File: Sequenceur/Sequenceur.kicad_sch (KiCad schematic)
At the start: 50 parts, among them J1 AudioJack2, J2 Jack-DC, SW1 SW_Push, SW2 SW_Rotary12, U1 NE555P, U2 4017, U3 OP07

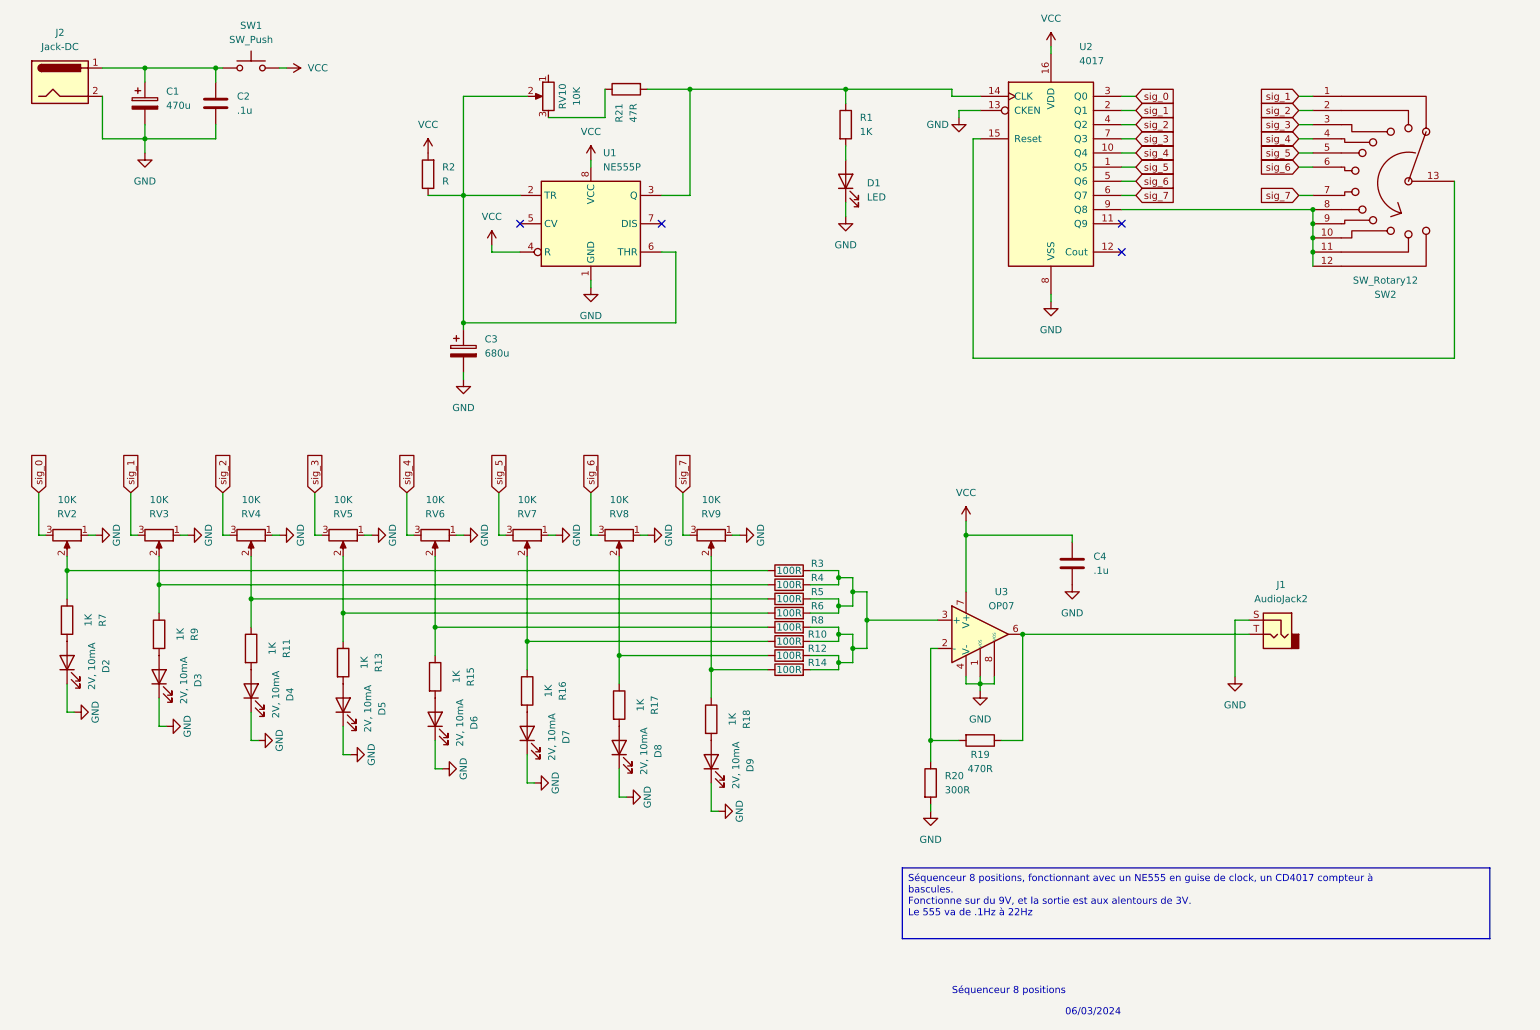
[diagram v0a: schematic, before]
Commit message: First real version of the PCB, as a 2 layer one, and with adapted footprints.
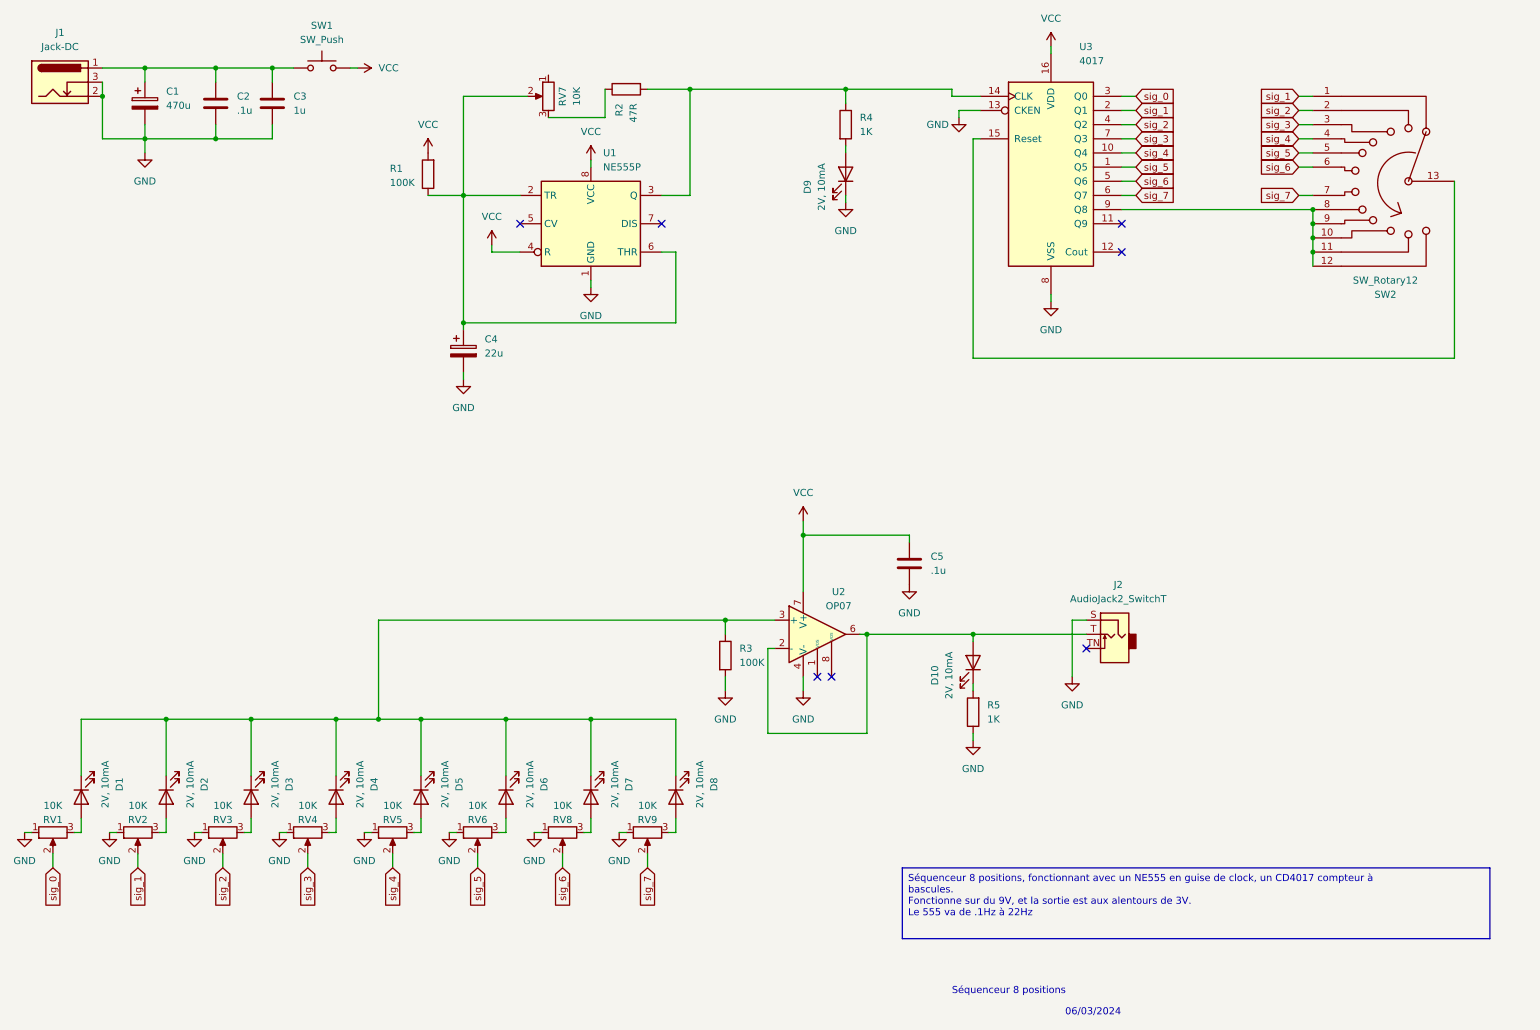
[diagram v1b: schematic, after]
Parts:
- removed D1: LED, LED_THT:LED_D3.0mm, symbol Device:LED
- removed J1: AudioJack2, Connector_Audio:Jack_6.35mm_Neutrik_NJ2FD-V_Vertical, symbol Connector_Audio:AudioJack2
- removed R10, R12, R14, R4, R6, R8: 100R, Resistor_SMD:R_0603_1608Metric, symbol Device:R
- removed R11, R13, R15, R16, R17, R18, R7, R9: 1K, Resistor_SMD:R_0603_1608Metric, symbol Device:R
- removed R19: 470R, Resistor_SMD:R_0805_2012Metric, symbol Device:R
- removed R20: 300R, Resistor_SMD:R_0805_2012Metric, symbol Device:R
- removed RV7: 10K, User_added:POTENTIOMETER_BOARDMNT_VERTICAL, symbol Device:R_Potentiometer
- added C3: 1u, Capacitor_SMD:C_0805_2012Metric, symbol Device:C
- added D10, D2: 2V, 10mA, LED_THT:LED_D5.0mm, symbol Device:LED
- added J2: AudioJack2_SwitchT, User_added:Jack_6.35_TTnS, symbol Connector_Audio:AudioJack2_SwitchT
- added RV2: 10K, User_added:POTENTIOMETER_BOARDMNT_VERTICAL, symbol Device:R_Potentiometer
- C4: renamed from C3; value 680u -> 22u; footprint Capacitor_THT:CP_Radial_D10.0mm_P5.00mm -> Capacitor_THT:CP_Radial_D5.0mm_P2.50mm
- D1: renamed from D2; footprint LED_THT:LED_D3.0mm -> LED_THT:LED_D5.0mm
- D3, D4, D5, D6, D7, D8, D9: footprint LED_THT:LED_D3.0mm -> LED_THT:LED_D5.0mm
- J1: renamed from J2; footprint Connector_BarrelJack:BarrelJack_SwitchcraftConxall_RAPC10U_Horizontal -> Connector_BarrelJack:BarrelJack_Horizontal; symbol Connector:Jack-DC -> Connector:Barrel_Jack_Switch
- R1: renamed from R2; value R -> 100K; footprint (none) -> Resistor_SMD:R_0603_1608Metric
- R3: value 100R -> 100K
- R5: value 100R -> 1K
- SW1: footprint User_added:PAD_2_std -> User_added:Switch_2pin
- renumbered C4 to C5, R21 to R2, R1 to R4, RV2 to RV1, RV10 to RV7, U3 to U2, U2 to U3
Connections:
- net GND: now also J1.3, R3.2, R5.1, C3.2, J2.S, RV2.1; no longer D1.1 (K), D3.1 (K), D4.1 (K), D5.1 (K), D6.1 (K), D7.1 (K), D8.1 (K), U2.1 (VOS), U2.8 (VOS)
- net sig_0: now also RV1.2; no longer RV1.3
- net sig_1: now also RV2.2; no longer RV3.3
- net sig_2: now also RV3.2; no longer RV4.3
- net sig_3: now also RV4.2; no longer RV5.3
- net sig_4: now also RV5.2; no longer RV6.3
- net sig_5: now also RV6.2
- net sig_6: now also RV8.2; no longer RV8.3
- net sig_7: now also RV9.2; no longer RV9.3
- net at R3.1: now also D1.1 (K), D3.1 (K), D4.1 (K), D5.1 (K), D6.1 (K), D7.1 (K), D8.1 (K), U2.3 (+), D2.1 (K); no longer RV1.2
- net at D4.2 (A): now also RV4.3
- net at D5.2 (A): now also RV5.3
- net at D7.2 (A): now also RV8.3
- net at D6.2 (A): now also RV6.3
- net at C1.1, C2.1, J1.1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: now also C3.1
- net at R4.2: now also D9.2 (A)
- net at U2.6: now also U2.2 (-), D10.2 (A), J2.T
- net at D8.2 (A): now also RV9.3
- net at D3.2 (A): now also RV3.3
- net at D1.2 (A): now also RV1.3
- new net: D2.2 (A), RV2.3
- new net: D10.1 (K), R5.2
- no-connect marks 4 -> 7
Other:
- moved on the sheet: C5, D1, RV1, SW1, U2
